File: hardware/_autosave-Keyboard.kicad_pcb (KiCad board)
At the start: 2 copper layers, 306.6 x 117.8 mm, 191 parts, among them J1 USB_C_Receptacle_USB2.0_16P, J2 Conn_01x04, SW1 SW_Push, SW2 SW_Push, U1 STM32F072CBTx, U2 XC6206PxxxMR

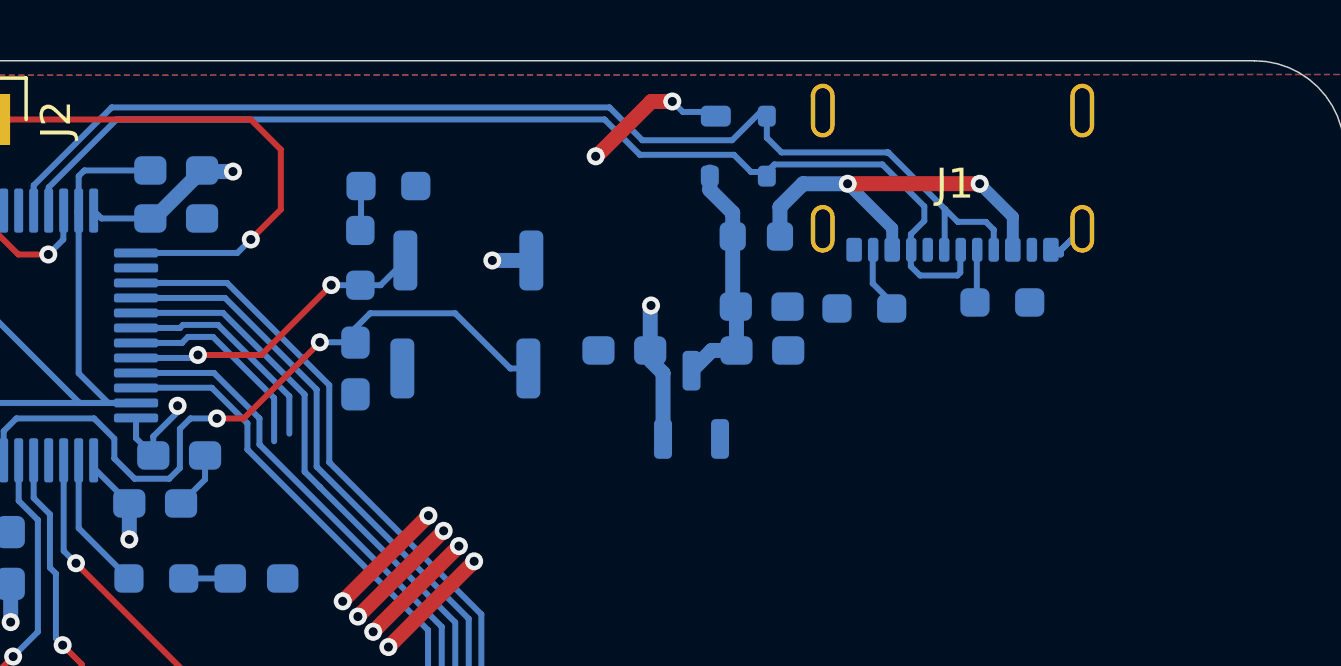
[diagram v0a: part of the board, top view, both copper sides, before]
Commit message: added OLED display + new libary for it
things to add:
test points
3.3v, 5v LED
fix some wiring
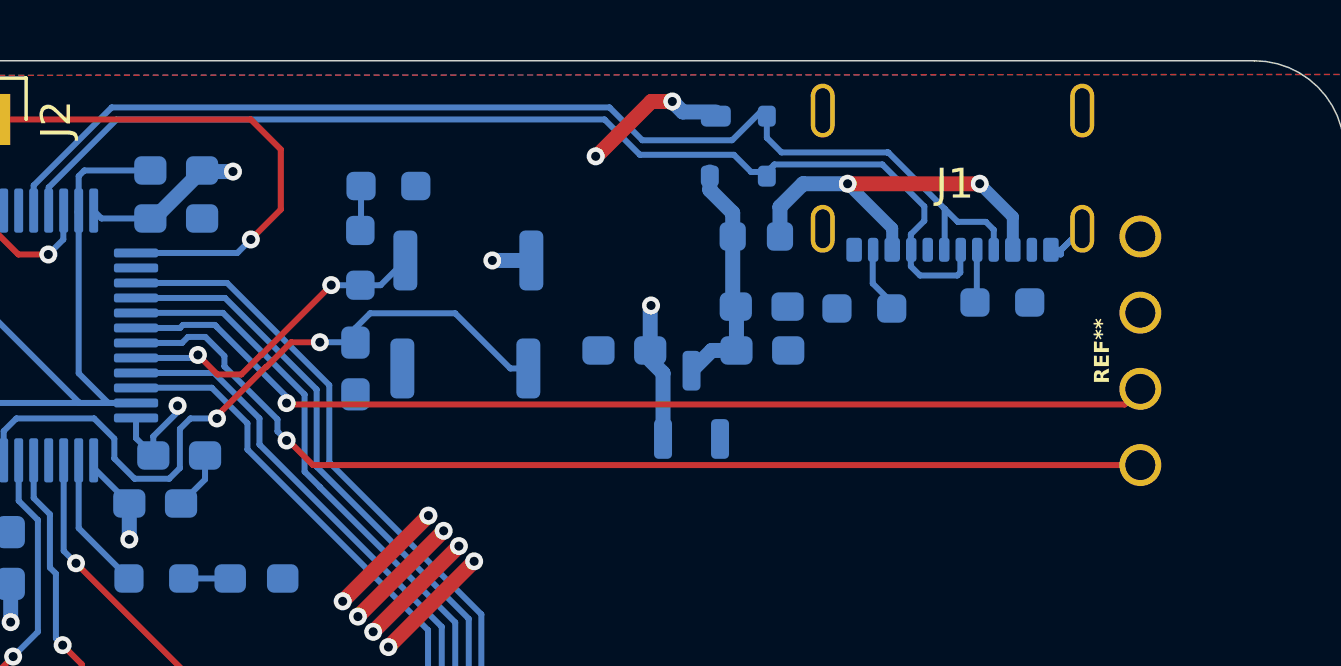
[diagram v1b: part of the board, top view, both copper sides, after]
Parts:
- added OL1: OLED, kbd:OLED, F.Cu at (300.4, 43.2)
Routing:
- net /SDA: track 6.97 -> 35.8 mm, vias 0 -> 1
- net /SCL: track 7.38 -> 35.0 mm, vias 0 -> 1
- net /BOOT0: track 10.6 -> 11.2 mm
